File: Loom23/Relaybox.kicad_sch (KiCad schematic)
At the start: 0 parts

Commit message: Signed-off-by: fst29 <fst29@cam.ac.uk>
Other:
- note added: "Relays here"
- note added: "Update this sheet when the actual schematic is done."
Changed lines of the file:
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@@
 (kicad_sch (version 20211123) (generator eeschema)
   (paper "A4")
+  (polyline (pts (xy 152.4 105.41) (xy 99.06 105.41))
+    (stroke (width 0) (type default) (color 0 0 0 0))
+  )
+  (polyline (pts (xy 99.06 59.69) (xy 99.06 105.41))
+    (stroke (width 0) (type default) (color 0 0 0 0))
+  )
+  (polyline (pts (xy 99.06 59.69) (xy 152.4 59.69))
+    (stroke (width 0) (type default) (color 0 0 0 0))
+  )
+  (polyline (pts (xy 152.4 59.69) (xy 152.4 105.41))
+    (stroke (width 0) (type default) (color 0 0 0 0))
+  )
+  (text "Update this sheet when the actual schematic is done.\n"
+    (at 101.6 33.02 0)
+    (effects (font (size 1.27 1.27)) (justify left bottom))
+  )
+  (text "Relays here" (at 118.11 77.47 0)
+    (effects (font (size 1.27 1.27)) (justify left bottom))
+  )
+  (hierarchical_label "Relayed Injectors" (shape input) (at 152.4 73.66 0)
+    (effects (font (size 1.27 1.27)) (justify left))
+  )
+  (hierarchical_label "Fuel pump enable (ECU)" (shape input) (at 99.06 76.2 180)
+    (effects (font (size 1.27 1.27)) (justify right))
+  )
+  (hierarchical_label "Paddle shifter" (shape input) (at 99.06 83.82 180)
+    (effects (font (size 1.27 1.27)) (justify right))
+  )
+  (hierarchical_label "RelayedSpark" (shape input) (at 152.4 66.04 0)
+    (effects (font (size 1.27 1.27)) (justify left))
+  )
+  (hierarchical_label "Relayed fuel pump" (shape input) (at 152.4 69.85 0)
+    (effects (font (size 1.27 1.27)) (justify left))
+  )
+  (hierarchical_label "+12V" (shape input) (at 99.06 62.23 180)
+    (effects (font (size 1.27 1.27)) (justify right))
+  )
+  (hierarchical_label "Shutdown signal" (shape input) (at 99.06 67.31 180)
+    (effects (font (size 1.27 1.27)) (justify right))
+  )
 )

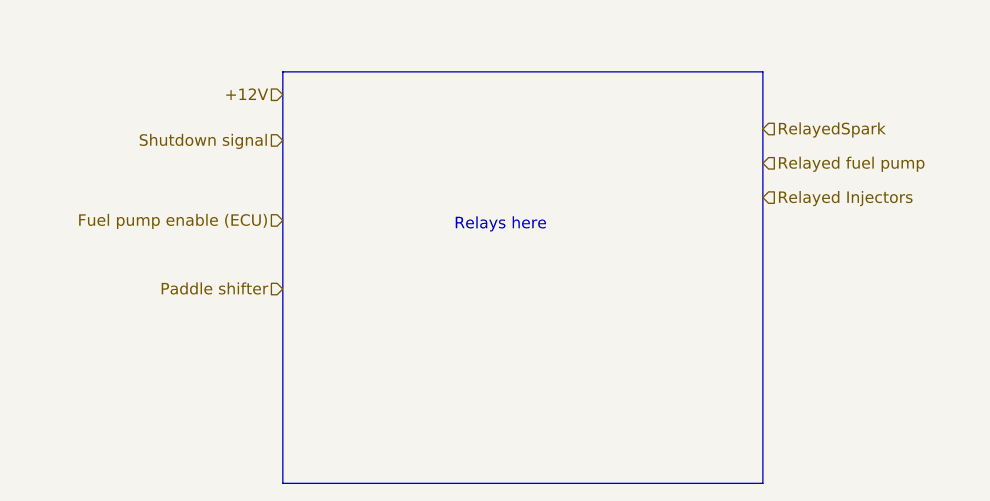
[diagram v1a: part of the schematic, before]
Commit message: Added fans and their control circuit. Added some wires.
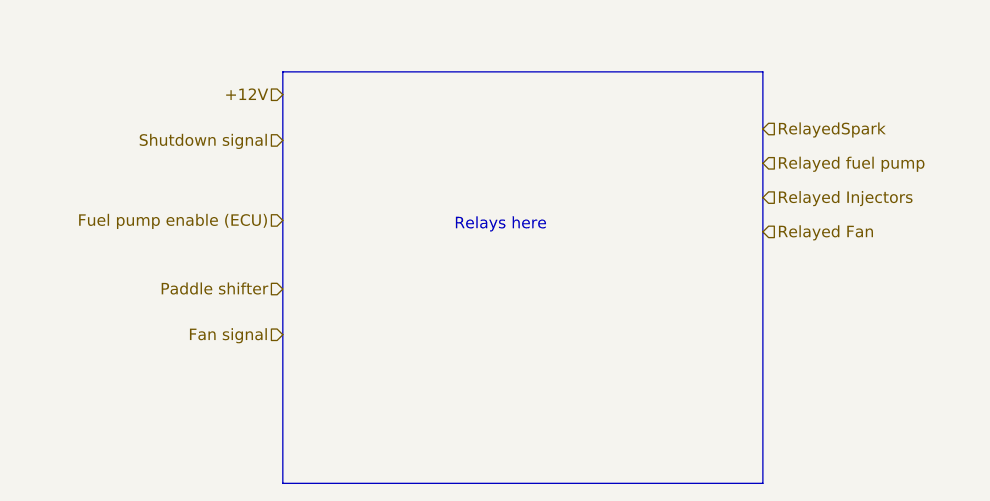
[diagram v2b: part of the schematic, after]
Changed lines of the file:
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@@
     (effects (font (size 1.27 1.27)) (justify left bottom))
+  )
+  (hierarchical_label "Relayed Fan" (shape input) (at 152.4 77.47 0)
+    (effects (font (size 1.27 1.27)) (justify left))
   )
   (hierarchical_label "Relayed Injectors" (shape input) (at 152.4 73.66 0)
@@
     (effects (font (size 1.27 1.27)) (justify left))
   )
+  (hierarchical_label "Fan signal" (shape input) (at 99.06 88.9 180)
+    (effects (font (size 1.27 1.27)) (justify right))
+  )
   (hierarchical_label "+12V" (shape input) (at 99.06 62.23 180)

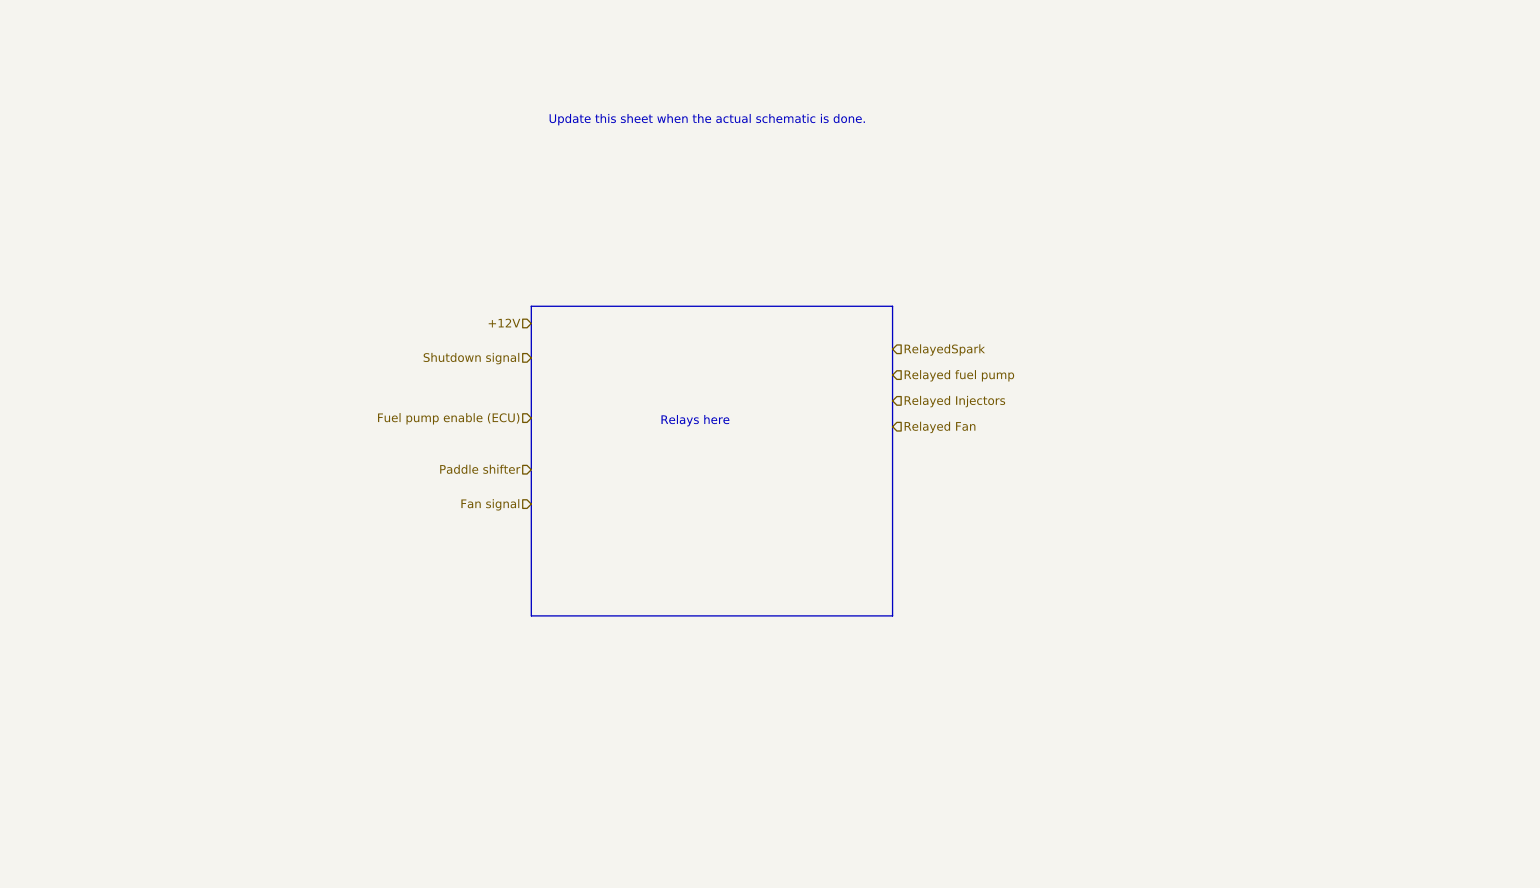
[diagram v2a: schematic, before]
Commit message: Added paddle shifter PCB and the relays.
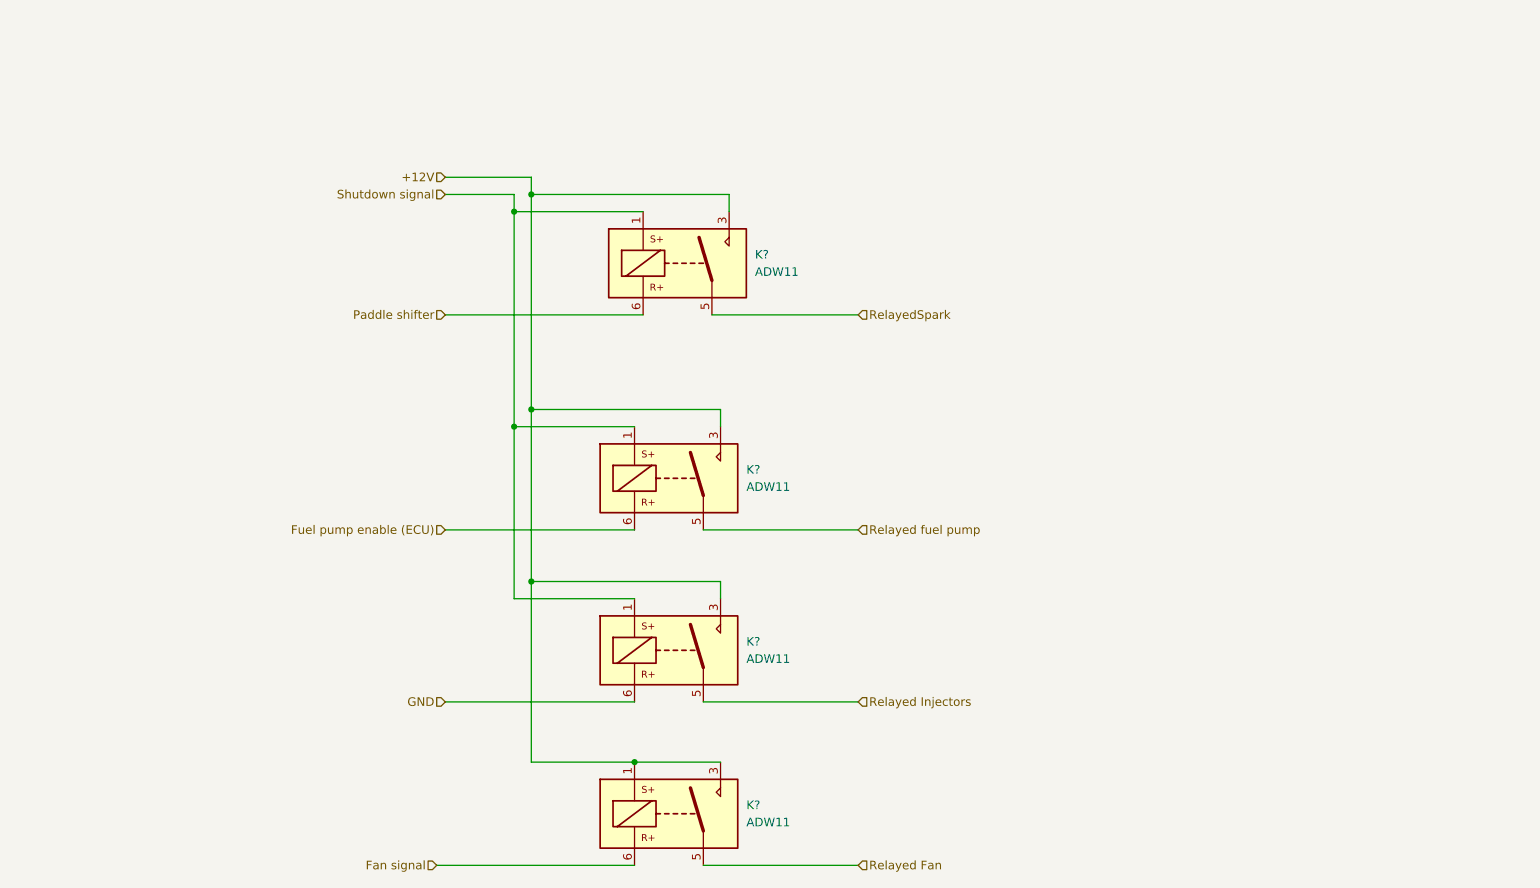
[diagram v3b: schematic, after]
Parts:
- added K? (x4): ADW11, Relay_THT:Relay_1P1T_NO_10x24x18.8mm_Panasonic_ADW11xxxxW_THT, symbol Relay:ADW11
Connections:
- net +12V: now also K?.1, K?.3, K?.3, K?.3, K?.3
- net Fan signal: now also K?.6
- net Fuel pump enable (ECU): now also K?.6
- net Paddle shifter: now also K?.6
- net Relayed Fan: now also K?.5
- net Relayed Injectors: now also K?.5
- net Relayed fuel pump: now also K?.5
- net RelayedSpark: now also K?.5
- net Shutdown signal: now also K?.1, K?.1, K?.1
- new net GND: K?.6
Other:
- note removed: "Relays here"
- note removed: "Update this sheet when the actual schematic is done."
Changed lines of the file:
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@@
 (kicad_sch (version 20211123) (generator eeschema)
   (paper "A4")
-  (polyline (pts (xy 152.4 105.41) (xy 99.06 105.41))
-    (stroke (width 0) (type default) (color 0 0 0 0))
-  )
-  (polyline (pts (xy 99.06 59.69) (xy 99.06 105.41))
-    (stroke (width 0) (type default) (color 0 0 0 0))
-  )
-  (polyline (pts (xy 99.06 59.69) (xy 152.4 59.69))
-    (stroke (width 0) (type default) (color 0 0 0 0))
-  )
-  (polyline (pts (xy 152.4 59.69) (xy 152.4 105.41))
-    (stroke (width 0) (type default) (color 0 0 0 0))
-  )
-  (text "Update this sheet when the actual schematic is done.\n"
-    (at 101.6 33.02 0)
-    (effects (font (size 1.27 1.27)) (justify left bottom))
-  )
-  (text "Relays here" (at 118.11 77.47 0)
-    (effects (font (size 1.27 1.27)) (justify left bottom))
-  )
-  (hierarchical_label "Relayed Fan" (shape input) (at 152.4 77.47 0)
-    (effects (font (size 1.27 1.27)) (justify left))
-  )
-  (hierarchical_label "Relayed Injectors" (shape input) (at 152.4 73.66 0)
-    (effects (font (size 1.27 1.27)) (justify left))
-  )
-  (hierarchical_label "Fuel pump enable (ECU)" (shape input) (at 99.06 76.2 180)
-    (effects (font (size 1.27 1.27)) (justify right))
-  )
-  (hierarchical_label "Paddle shifter" (shape input) (at 99.06 83.82 180)
-    (effects (font (size 1.27 1.27)) (justify right))
-  )
-  (hierarchical_label "RelayedSpark" (shape input) (at 152.4 66.04 0)
-    (effects (font (size 1.27 1.27)) (justify left))
-  )
-  (hierarchical_label "Relayed fuel pump" (shape input) (at 152.4 69.85 0)
-    (effects (font (size 1.27 1.27)) (justify left))
-  )
-  (hierarchical_label "Fan signal" (shape input) (at 99.06 88.9 180)
-    (effects (font (size 1.27 1.27)) (justify right))
-  )
-  (hierarchical_label "+12V" (shape input) (at 99.06 62.23 180)
-    (effects (font (size 1.27 1.27)) (justify right))
-  )
-  (hierarchical_label "Shutdown signal" (shape input) (at 99.06 67.31 180)
-    (effects (font (size 1.27 1.27)) (justify right))
+  (junction (at 99.06 74.93) (diameter 0) (color 0 0 0 0)
+  )
+  (junction (at 114.3 127) (diameter 0) (color 0 0 0 0)
+  )
+  (junction (at 96.52 45.72) (diameter 0) (color 0 0 0 0)
+  )
+  (junction (at 99.06 100.33) (diameter 0) (color 0 0 0 0)
+  )
+  (junction (at 99.06 43.18) (diameter 0) (color 0 0 0 0)
+  )
+  (junction (at 96.52 77.47) (diameter 0) (color 0 0 0 0)
+  )
+  (wire (pts (xy 96.52 43.18) (xy 96.52 45.72))
+    (stroke (width 0) (type default) (color 0 0 0 0))
+  )
+  (wire (pts (xy 99.06 43.18) (xy 99.06 74.93))
+    (stroke (width 0) (type default) (color 0 0 0 0))
+  )
+  (wire (pts (xy 125.73 60.96) (xy 147.32 60.96))
+    (stroke (width 0) (type default) (color 0 0 0 0))
+  )
+  (wire (pts (xy 96.52 45.72) (xy 96.52 77.47))
+    (stroke (width 0) (type default) (color 0 0 0 0))
+  )
+  (wire (pts (xy 86.36 92.71) (xy 114.3 92.71))
+    (stroke (width 0) (type default) (color 0 0 0 0))
+  )
+  (wire (pts (xy 99.06 74.93) (xy 127 74.93))
+    (stroke (width 0) (type default) (color 0 0 0 0))
+  )
+  (wire (pts (xy 99.06 100.33) (xy 99.06 127))
+    (stroke (width 0) (type default) (color 0 0 0 0))
+  )
+  (wire (pts (xy 124.46 142.24) (xy 147.32 142.24))
+    (stroke (width 0) (type default) (color 0 0 0 0))
+  )
+  (wire (pts (xy 86.36 118.11) (xy 114.3 118.11))
+    (stroke (width 0) (type default) (color 0 0 0 0))
+  )
+  (wire (pts (xy 99.06 40.64) (xy 99.06 43.18))
+    (stroke (width 0) (type default) (color 0 0 0 0))
+  )
+  (wire (pts (xy 124.46 118.11) (xy 147.32 118.11))
+    (stroke (width 0) (type default) (color 0 0 0 0))
+  )
+  (wire (pts (xy 124.46 92.71) (xy 147.32 92.71))
+    (stroke (width 0) (type default) (color 0 0 0 0))
+  )
+  (wire (pts (xy 96.52 102.87) (xy 114.3 102.87))
+    (stroke (width 0) (type default) (color 0 0 0 0))
+  )
+  (wire (pts (xy 86.36 60.96) (xy 115.57 60.96))
+    (stroke (width 0) (type default) (color 0 0 0 0))
+  )
+  (wire (pts (xy 127 77.47) (xy 127 74.93))
+    (stroke (width 0) (type default) (color 0 0 0 0))
+  )
+  (wire (pts (xy 99.06 74.93) (xy 99.06 100.33))
+    (stroke (width 0) (type default) (color 0 0 0 0))
+  )
+  (wire (pts (xy 128.27 45.72) (xy 128.27 43.18))
+    (stroke (width 0) (type default) (color 0 0 0 0))
+  )
+  (wire (pts (xy 85.09 142.24) (xy 114.3 142.24))
+    (stroke (width 0) (type default) (color 0 0 0 0))
+  )
+  (wire (pts (xy 115.57 45.72) (xy 96.52 45.72))
+    (stroke (width 0) (type default) (color 0 0 0 0))
+  )
+  (wire (pts (xy 99.06 100.33) (xy 127 100.33))
+    (stroke (width 0) (type default) (color 0 0 0 0))
+  )
+  (wire (pts (xy 99.06 127) (xy 114.3 127))
+    (stroke (width 0) (type default) (color 0 0 0 0))
+  )
+  (wire (pts (xy 96.52 77.47) (xy 114.3 77.47))
+    (stroke (width 0) (type default) (color 0 0 0 0))
+  )
+  (wire (pts (xy 86.36 43.18) (xy 96.52 43.18))
+    (stroke (width 0) (type default) (color 0 0 0 0))
+  )
+  (wire (pts (xy 86.36 40.64) (xy 99.06 40.64))
+    (stroke (width 0) (type default) (color 0 0 0 0))
+  )
+  (wire (pts (xy 127 102.87) (xy 127 100.33))
+    (stroke (width 0) (type default) (color 0 0 0 0))
+  )
+  (wire (pts (xy 114.3 127) (xy 127 127))
+    (stroke (width 0) (type default) (color 0 0 0 0))
+  )
+  (wire (pts (xy 99.06 43.18) (xy 128.27 43.18))
+    (stroke (width 0) (type default) (color 0 0 0 0))
+  )
+  (wire (pts (xy 96.52 77.47) (xy 96.52 102.87))
+    (stroke (width 0) (type default) (color 0 0 0 0))
+  )
+  (hierarchical_label "Relayed Fan" (shape input) (at 147.32 142.24 0)
+    (effects (font (size 1.27 1.27)) (justify left))
+  )
+  (hierarchical_label "Relayed Injectors" (shape input) (at 147.32 118.11 0)
+    (effects (font (size 1.27 1.27)) (justify left))
+  )
+  (hierarchical_label "Fuel pump enable (ECU)" (shape input) (at 86.36 92.71 180)
+    (effects (font (size 1.27 1.27)) (justify right))
+  )
+  (hierarchical_label "Paddle shifter" (shape input) (at 86.36 60.96 180)
+    (effects (font (size 1.27 1.27)) (justify right))
+  )
+  (hierarchical_label "RelayedSpark" (shape input) (at 147.32 60.96 0)
+    (effects (font (size 1.27 1.27)) (justify left))
+  )
+  (hierarchical_label "Relayed fuel pump" (shape input) (at 147.32 92.71 0)
+    (effects (font (size 1.27 1.27)) (justify left))
+  )
+  (hierarchical_label "Fan signal" (shape input) (at 85.09 142.24 180)
+    (effects (font (size 1.27 1.27)) (justify right))
+  )
+  (hierarchical_label "+12V" (shape input) (at 86.36 40.64 180)
+    (effects (font (size 1.27 1.27)) (justify right))
+  )
+  (hierarchical_label "Shutdown signal" (shape input) (at 86.36 43.18 180)
+    (effects (font (size 1.27 1.27)) (justify right))
+  )
+  (hierarchical_label "GND" (shape input) (at 86.36 118.11 180)
+    (effects (font (size 1.27 1.27)) (justify right))
+  )
+  (symbol (lib_id "Relay:ADW11") (at 119.38 134.62 0) (unit 1)
+    (in_bom yes) (on_board yes) (fields_autoplaced)
+    (property "Reference" "K?" (id 0) (at 130.81 133.3499 0)
+      (effects (font (size 1.27 1.27)) (justify left))
+    )
+    (property "Value" "ADW11" (id 1) (at 130.81 135.8899 0)
+      (effects (font (size 1.27 1.27)) (justify left))
+    )
+    (property "Footprint" "Relay_THT:Relay_1P1T_NO_10x24x18.8mm_Panasonic_ADW11xxxxW_THT" (id 2) (at 153.035 135.89 0)
+      (effects (font (size 1.27 1.27)) hide)
+    )
+    (property "Datasheet" "https://www.panasonic-electric-works.com/pew/es/downloads/ds_dw_hl_en.pdf" (id 3) (at 119.38 134.62 0)
+      (effects (font (size 1.27 1.27)) hide)
+    )
+    (pin "1")
+    (pin "3")
+    (pin "5")
+    (pin "6")
+  )
+  (symbol (lib_id "Relay:ADW11") (at 119.38 85.09 0) (unit 1)
+    (in_bom yes) (on_board yes) (fields_autoplaced)
+    (property "Reference" "K?" (id 0) (at 130.81 83.8199 0)
+      (effects (font (size 1.27 1.27)) (justify left))
+    )
+    (property "Value" "ADW11" (id 1) (at 130.81 86.3599 0)
+      (effects (font (size 1.27 1.27)) (justify left))
+    )
+    (property "Footprint" "Relay_THT:Relay_1P1T_NO_10x24x18.8mm_Panasonic_ADW11xxxxW_THT" (id 2) (at 153.035 86.36 0)
+      (effects (font (size 1.27 1.27)) hide)
+    )
+    (property "Datasheet" "https://www.panasonic-electric-works.com/pew/es/downloads/ds_dw_hl_en.pdf" (id 3) (at 119.38 85.09 0)
+      (effects (font (size 1.27 1.27)) hide)
+    )
+    (pin "1")
+    (pin "3")
+    (pin "5")
+    (pin "6")
+  )
+  (symbol (lib_id "Relay:ADW11") (at 119.38 110.49 0) (unit 1)
+    (in_bom yes) (on_board yes) (fields_autoplaced)
+    (property "Reference" "K?" (id 0) (at 130.81 109.2199 0)
+      (effects (font (size 1.27 1.27)) (justify left))
+    )
+    (property "Value" "ADW11" (id 1) (at 130.81 111.7599 0)
+      (effects (font (size 1.27 1.27)) (justify left))
+    )
+    (property "Footprint" "Relay_THT:Relay_1P1T_NO_10x24x18.8mm_Panasonic_ADW11xxxxW_THT" (id 2) (at 153.035 111.76 0)
+      (effects (font (size 1.27 1.27)) hide)
+    )
+    (property "Datasheet" "https://www.panasonic-electric-works.com/pew/es/downloads/ds_dw_hl_en.pdf" (id 3) (at 119.38 110.49 0)
+      (effects (font (size 1.27 1.27)) hide)
+    )
+    (pin "1")
+    (pin "3")
+    (pin "5")
+    (pin "6")
+  )
+  (symbol (lib_id "Relay:ADW11") (at 120.65 53.34 0) (unit 1)
+    (in_bom yes) (on_board yes) (fields_autoplaced)
+    (property "Reference" "K?" (id 0) (at 132.08 52.0699 0)
+      (effects (font (size 1.27 1.27)) (justify left))
+    )
+    (property "Value" "ADW11" (id 1) (at 132.08 54.6099 0)
+      (effects (font (size 1.27 1.27)) (justify left))
+    )
+    (property "Footprint" "Relay_THT:Relay_1P1T_NO_10x24x18.8mm_Panasonic_ADW11xxxxW_THT" (id 2) (at 154.305 54.61 0)
+      (effects (font (size 1.27 1.27)) hide)
+    )
+    (property "Datasheet" "https://www.panasonic-electric-works.com/pew/es/downloads/ds_dw_hl_en.pdf" (id 3) (at 120.65 53.34 0)
+      (effects (font (size 1.27 1.27)) hide)
+    )
+    (pin "1")
+    (pin "3")
+    (pin "5")
+    (pin "6")
   )
 )
